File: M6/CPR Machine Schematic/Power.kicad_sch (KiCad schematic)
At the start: 53 parts, among them J1 Battery 22.2V IN, J16 Motor Driver, J2 Power Switch, J3 5V Spare Headers, J4 GND Spare Headers, J5 3V3 Spare Headers, J6 12 Spare headers, J7 Battery Spare headers, Q1 DMMT5401 PNP, Q2 SSM3J332R, Q3 DMG2305UX-EV, Q4 DMMT5401 PNP, SW1 SW_SPST, U1 3.3V Buck, U2 12V Buck, U3 MAX42403AFLB+

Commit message: Condensed Header Pins
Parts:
- removed J3: 5V Spare Headers, Connector_PinHeader_2.54mm:PinHeader_1x05_P2.54mm_Vertical, symbol Connector:Conn_01x05_Pin
- removed J5: 3V3 Spare Headers, Connector_PinHeader_2.54mm:PinHeader_1x03_P2.54mm_Vertical, symbol Connector:Conn_01x03_Pin
- removed J6: 12 Spare headers, Connector_PinHeader_2.54mm:PinHeader_1x02_P2.54mm_Vertical, symbol Connector:Conn_01x02_Pin
- removed J7: Battery Spare headers, Connector_PinHeader_2.54mm:PinHeader_1x02_P2.54mm_Vertical, symbol Connector:Conn_01x02_Pin
- added C6: 10 nF, Capacitor_SMD:C_1206_3216Metric_Pad1.33x1.80mm_HandSolder, symbol Device:C
- added J3: +V Spare Headers, Connector_PinHeader_2.54mm:PinHeader_1x12_P2.54mm_Vertical, symbol Connector:Conn_01x12_Pin
- renumbered R2 to R1, R1 to R2, U2 to U1, U1 to U2
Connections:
- net +12V: now also J3.10 (Pin_10), J3.9 (Pin_9); no longer Contactor1.2, F3.1
- net +22.2V: now also J3.11 (Pin_11), J3.12 (Pin_12)
- net +3.3V: now also J3.6 (Pin_6), J3.7 (Pin_7), J3.8 (Pin_8)
- net +5V: now also J3.1 (Pin_1), J3.2 (Pin_2), J3.3 (Pin_3), J3.4 (Pin_4), J3.5 (Pin_5)
- net Reg OUT: now also C6.2
- net at Q3.1, Q4.4, R11.1: now also C6.1
- new net: Contactor1.2, F3.1

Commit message: Part Inventory
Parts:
- C1, CIN1, CIN2: Notes Have: 4 -> Have: 9
- C2, C3, C4: Notes (none) -> Have: 10+; now in the parts list
- C5, F1, L1, R4: Notes (none) -> Have: 5; now in the parts list
- COUT1, COUT2: Notes (none) -> Have: 4
- F3: now in the parts list
- J1, J2, J3: now left out of the parts list
- LED1, LED2, LED3, LED4: Notes Have: 2 -> Have: 10+
- Q1, Q4, R7: Notes (none) -> Have: 2; now in the parts list
- Q2, Q3: Notes (none) -> Have: 2
- R1, R11, R6: Notes (none) -> Have: 4; now in the parts list
- R3: Notes (none) -> Have: 6; now in the parts list
- R8: Notes (none) -> Have: 7; now in the parts list
- U1: Notes (none) -> Have: 0; now in the parts list
- U2, U3: Notes Have: 1 -> Have: 2

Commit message: Replace COUT with one in stock
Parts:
- COUT1, COUT2: digikey 490-5312-1-ND -> 490-GRM32ER71A476KE15KCT-ND
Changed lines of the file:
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@@
 			)
 		)
-		(property "digikey" "490-5312-1-ND"
+		(property "digikey" "490-GRM32ER71A476KE15KCT-ND"
 			(at 45.72 82.55 0)
 			(effects
@@
 			)
 		)
-		(property "digikey" "490-5312-1-ND"
+		(property "digikey" "490-GRM32ER71A476KE15KCT-ND"
 			(at 31.75 82.55 0)
 			(effects

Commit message: GND testpoint, Main 0V diode redesign, Geograph Redesignate
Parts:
- added TP5: GND, TestPoint:TestPoint_THTPad_4.0x4.0mm_Drill2.0mm, symbol Connector:TestPoint
- J1, J2: footprint Connector_AMASS:AMASS_XT30PW-M_1x02_P2.50mm_Horizontal -> Connector_AMASS:AMASS_XT30PW-F_1x02_P2.50mm_Horizontal
- TP4: footprint TestPoint:TestPoint_THTPad_4.0x4.0mm_Drill2.0mm -> TestPoint:TestPoint_THTPad_D4.0mm_Drill2.0mm
- renumbered C6 to C5, C5 to C6, J4 to J3, J3 to J4, LED2 to LED1, LED1 to LED2, R2 to R1, R1 to R2, R9 to R6, R8 to R7, R6 to R8, R7 to R9, U2 to U1, U1 to U2
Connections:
- net Battery +: now also J1.2 (Pin_2); no longer J1.1 (Pin_1)
- net GND: now also J1.1 (Pin_1), TP5.1; no longer J1.2 (Pin_2)
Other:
- moved on the sheet: J1, TP1, TP2, TP3, TP4

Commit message: Swap out out-of-stock parts
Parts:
- C6: digikey 1292-1206N470J102CT-ND -> 732-7874-1-ND
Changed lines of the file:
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@@
 			)
 		)
-		(property "Datasheet" "http://www.passivecomponent.com/wp-content/uploads/datasheet/WTC_MLCC_Middle_and_High_Voltage.pdf"
+		(property "Datasheet" "https://www.digikey.com/en/products/detail/w%C3%BCrth-elektronik/885012008021/5453729"
 			(at 29.21 95.25 0)
 			(effects
@@
 			)
 		)
-		(property "digikey" "1292-1206N470J102CT-ND"
+		(property "digikey" "732-7874-1-ND"
 			(at 29.21 95.25 0)
 			(effects

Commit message: Start of ESD
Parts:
- added D1: D_TVS, Diode_SMD:D_SOD-323_HandSoldering, symbol Device:D_TVS
- added D10: D_TVS, Diode_SMD:D_SOD-882, symbol Device:D_Zener
- added D5, D6, D7, D8: D_TVS, Diode_SMD:D_SMA, symbol Device:D_Zener
- added D9: D_TVS, Diode_SMD:D_SOD-323F, symbol Device:D_Zener
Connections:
- net +12V: now also D5.1 (K), D6.1 (K)
- net +22.2V: now also D8.1 (K)
- net +3.3V: now also D10.1 (K)
- net +5V: now also D9.1 (K)
- net Battery +: now also D1.2 (A2)
- net From Switch: now also D7.1 (K)
- net GND: now also D1.1 (A1), D10.2 (A), D5.2 (A), D6.2 (A), D7.2 (A), D8.2 (A), D9.2 (A)
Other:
- moved on the sheet: J1, J2, J3, J4, U2

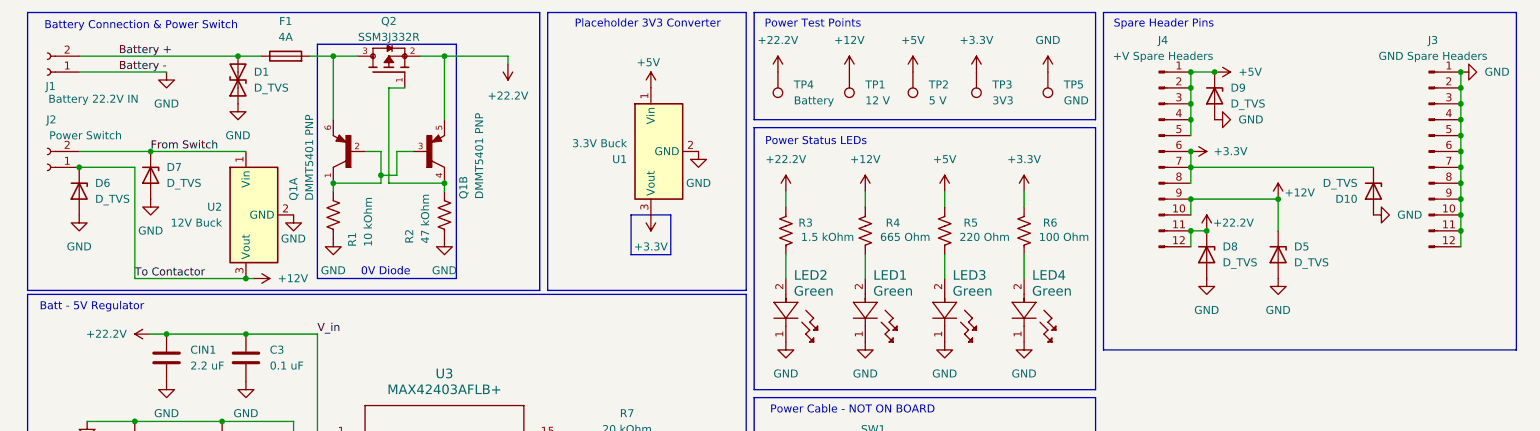
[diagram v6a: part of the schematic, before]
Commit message: ESD Protection
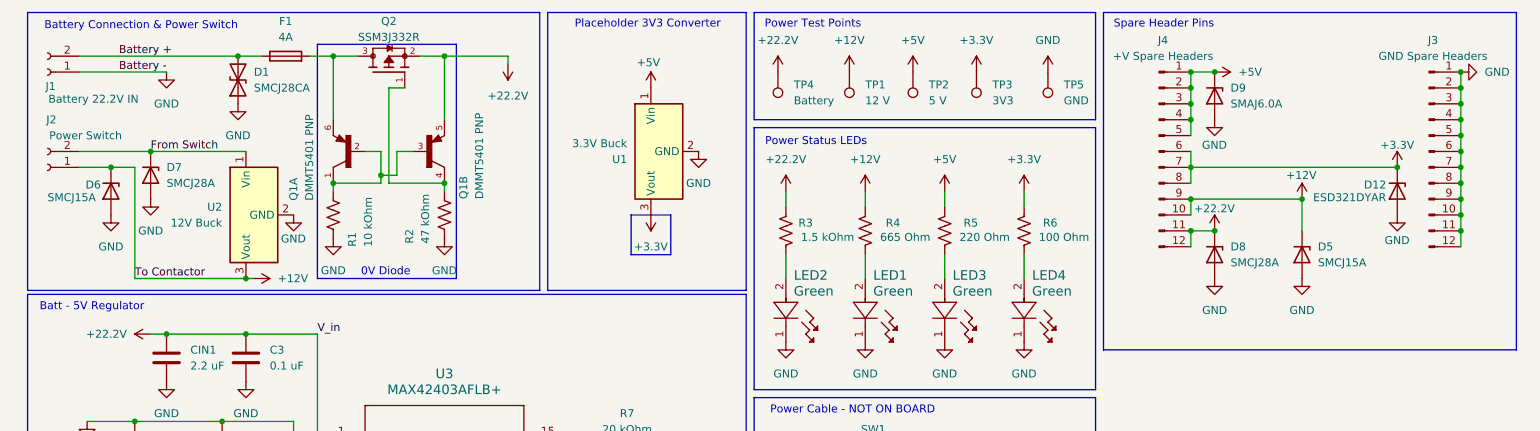
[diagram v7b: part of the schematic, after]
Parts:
- removed D10: D_TVS, Diode_SMD:D_SOD-882, symbol Device:D_Zener
- added D12: ESD321DYAR, Diode_SMD:D_SOD-523, symbol Diode:PTVS5V0Z1USK
- D1: value D_TVS -> SMCJ28CA; footprint Diode_SMD:D_SOD-323_HandSoldering -> Diode_SMD:D_SMC; digikey DF2B36FUH3FCT-ND -> SMCJ28CALFCT-ND
- D5, D6: value D_TVS -> SMCJ15A; footprint Diode_SMD:D_SMA -> Diode_SMD:D_SMC; digikey SMAJ13ALFCT-ND -> SMCJ15ALFCT-ND
- D7, D8: value D_TVS -> SMCJ28A; footprint Diode_SMD:D_SMA -> Diode_SMD:D_SMC; digikey SMAJ28ALFCT-ND -> SMCJ28ALFCT-ND
- D9: value D_TVS -> SMAJ6.0A; footprint Diode_SMD:D_SOD-323F -> Diode_SMD:D_SMA; digikey 31-SD05A-7CT-ND -> SMAJ6.0ALFCT-ND
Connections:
- net +3.3V: now also D12.1 (K)
- net GND: now also D12.2 (A)
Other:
- moved on the sheet: D5
